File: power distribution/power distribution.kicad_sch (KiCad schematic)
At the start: 211 parts, among them J1 HEATER6, J10 TH0, J11 TH4, J13 HEATER4, J14 TH1, J15 TH5, J17 Conn_01x02_Socket, J18 Conn_01x02_Socket, J19 HEATER5, J2 HEATER0, J20 TH2, J21 TH6, J22 TH3, J23 TH7, J3 HEATER7, J4 SWD, J5 HEATER1, J6 HEATER2, J7 UART, J8 USB_C_Receptacle_USB2.0_14P, J9 HEATER3, Q1 AOD4184A, Q2 AOD4184A, Q3 AOD4184A, Q4 AOD4184A, Q5 AOD4184A, Q6 AOD4184A, Q7 AOD4184A, Q8 AOD4184A, SW1 SW_Push, SW2 SW_Push, U1 TPS54202DDC, U10 UCC27511ADBV, U11 TLV73333PDBV, U12 TLV73333PDBV, U13 UCC27511ADBV, U14 UCC27511ADBV, U15 UCC27511ADBV, U2 UCC27511ADBV, U3 UCC27511ADBV, U4 STM32F030K6Tx, U5 TPS54202DDC, U6 UCC27511ADBV, U7 UCC27511ADBV, U8 SRV05-4, U9 CH340E, Y1 24MHz

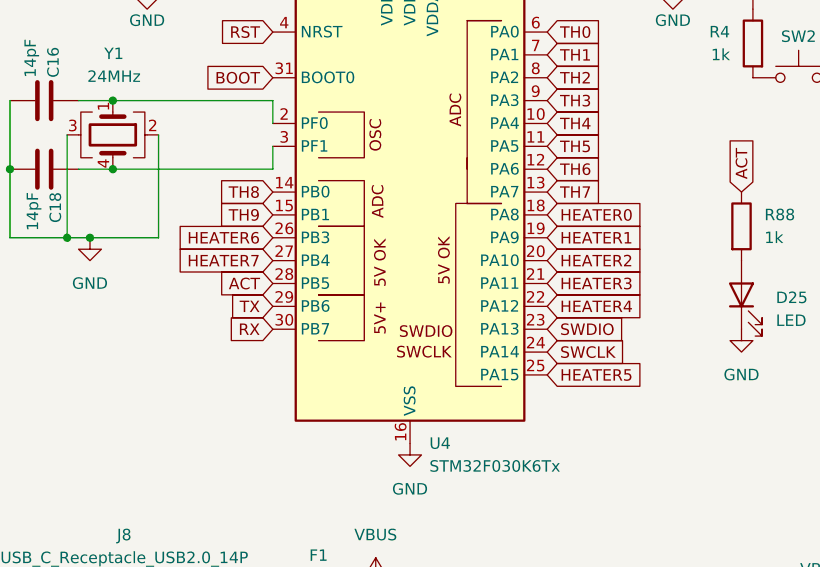
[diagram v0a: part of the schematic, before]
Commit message: fix: fixed uart connections, usb flashing requires flashing via UART on PA9/PA10
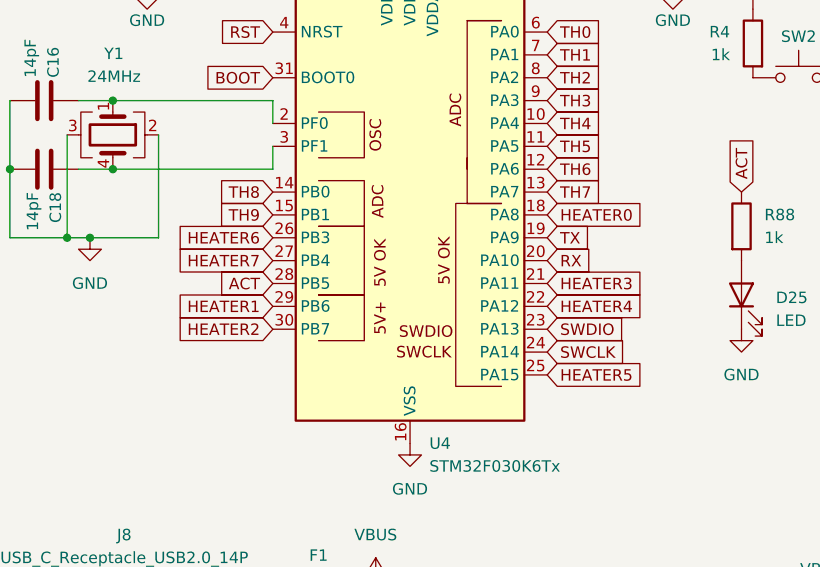
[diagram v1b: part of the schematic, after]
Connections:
- net HEATER1: now also U4.29 (PB6); no longer U4.19 (PA9)
- net HEATER2: now also U4.30 (PB7); no longer U4.20 (PA10)
- net RX: now also U4.20 (PA10); no longer U4.30 (PB7)
- net TX: now also U4.19 (PA9); no longer U4.29 (PB6)
